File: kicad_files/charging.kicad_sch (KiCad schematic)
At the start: 2 parts, among them U2 BQ24650, U3 TL431DBZ

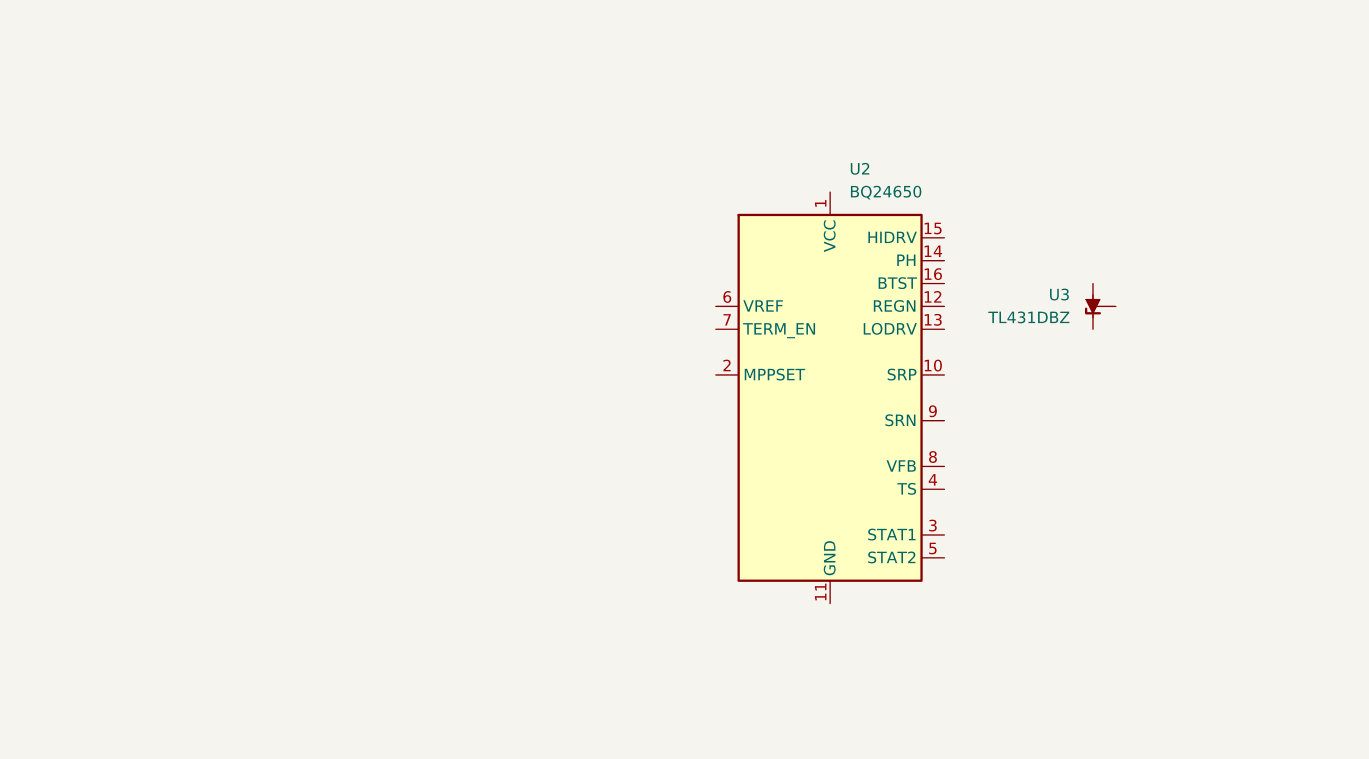
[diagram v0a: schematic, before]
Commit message: Some progress on charging schematic
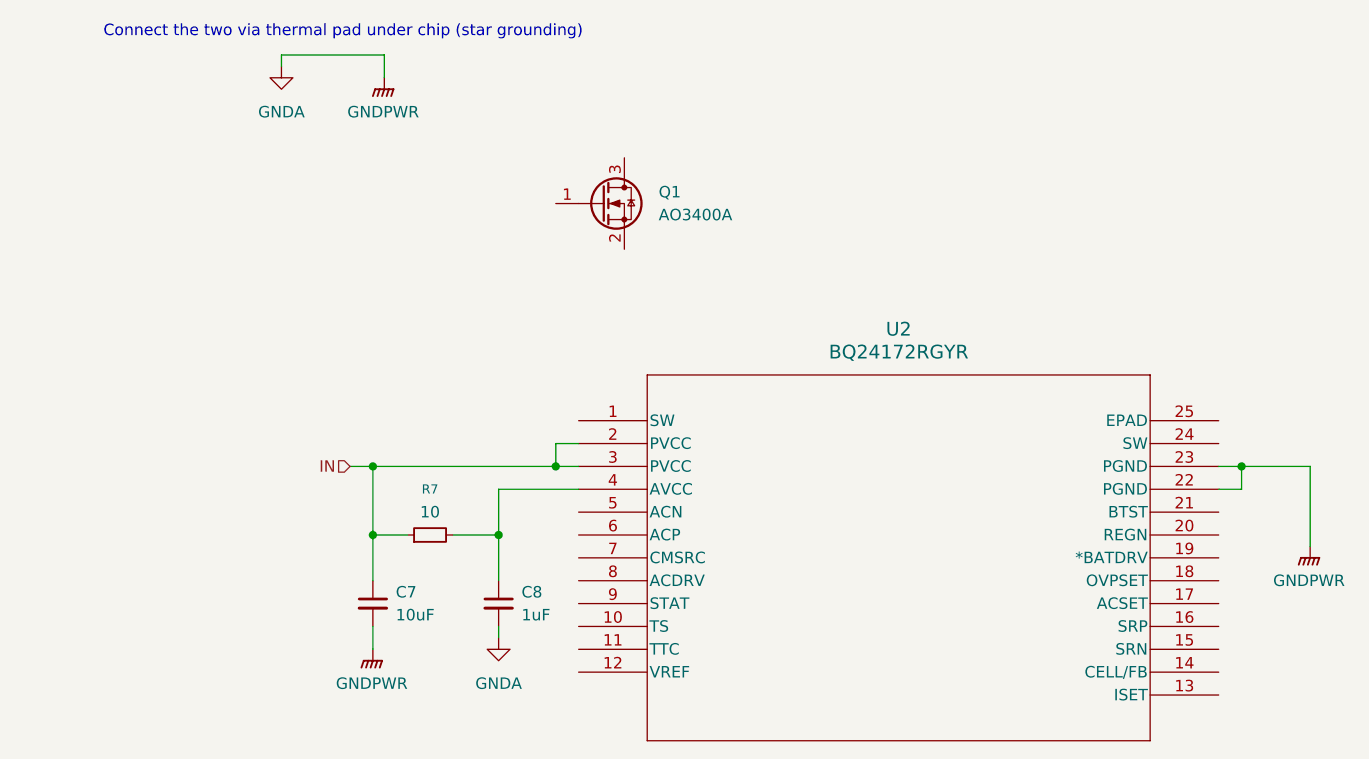
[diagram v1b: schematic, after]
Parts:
- removed U2: BQ24650, Package_DFN_QFN:Texas_RVA_VQFN-16-1EP_3.5x3.5mm_P0.5mm_EP2.14x2.14mm_ThermalVias, symbol Battery_Management:BQ24650
- removed U3: TL431DBZ, Package_TO_SOT_SMD:SOT-23, symbol Reference_Voltage:TL431DBZ
- added C7: 10uF, symbol Device:C_Small
- added C8: 1uF, symbol Device:C_Small
- added Q1: AO3400A, Package_TO_SOT_SMD:SOT-23, symbol Transistor_FET:AO3400A
- added R7: 10, symbol Device:R_Small
- added U2: BQ24172RGYR, RGY24_2P05X3P1, symbol !symbols:BQ24172RGYR
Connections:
- new net: C8.1, R7.2, U2.4 (AVCC)
- new net GNDA: C7.2, C8.2, U2.22 (PGND), U2.23 (PGND)
- new net IN: C7.1, R7.1, U2.2 (PVCC), U2.3 (PVCC)
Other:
- note added: "Connect the two via thermal pad under chip (star grounding)"

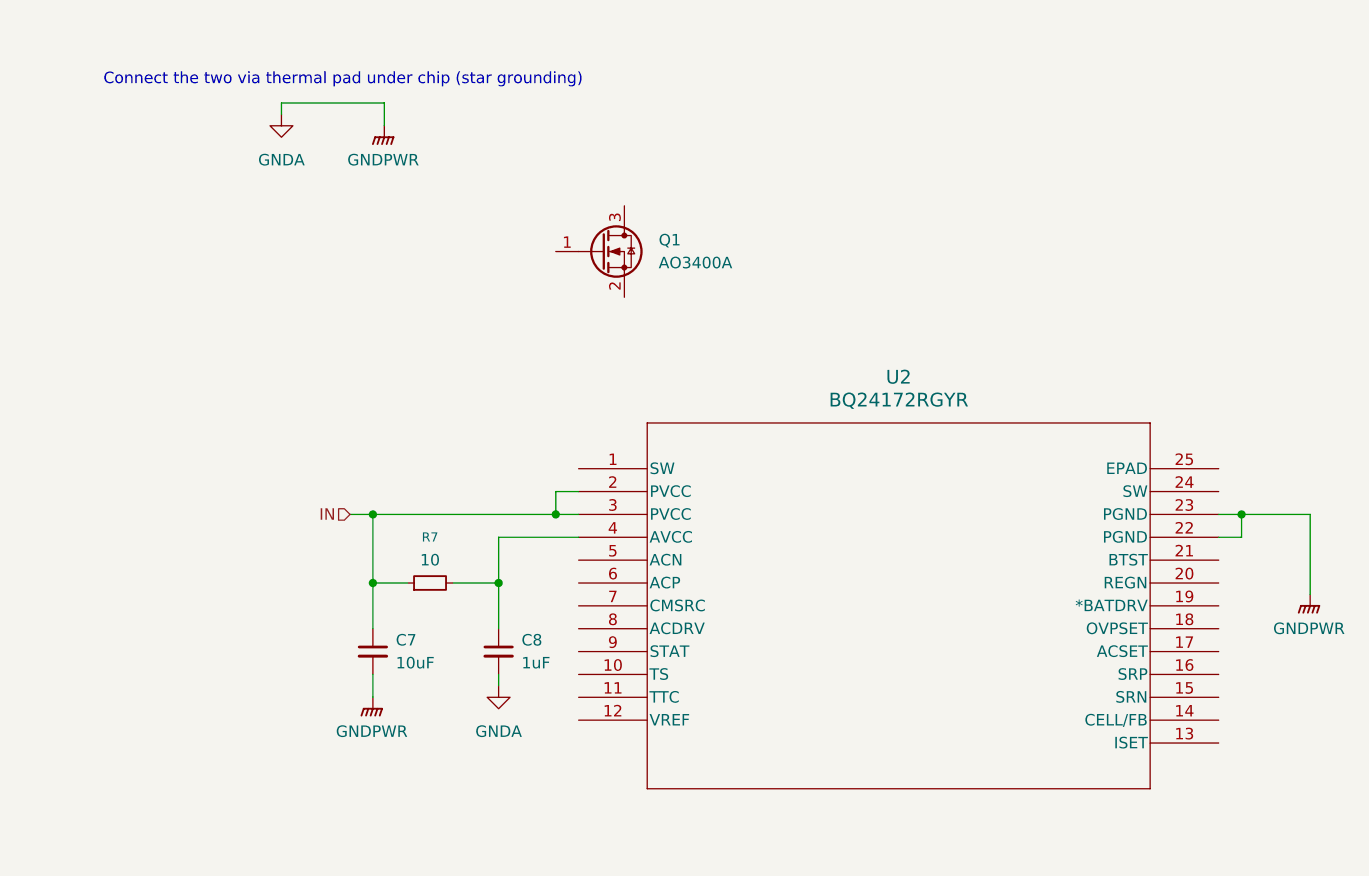
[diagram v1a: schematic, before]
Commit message: More progress on charging schematic
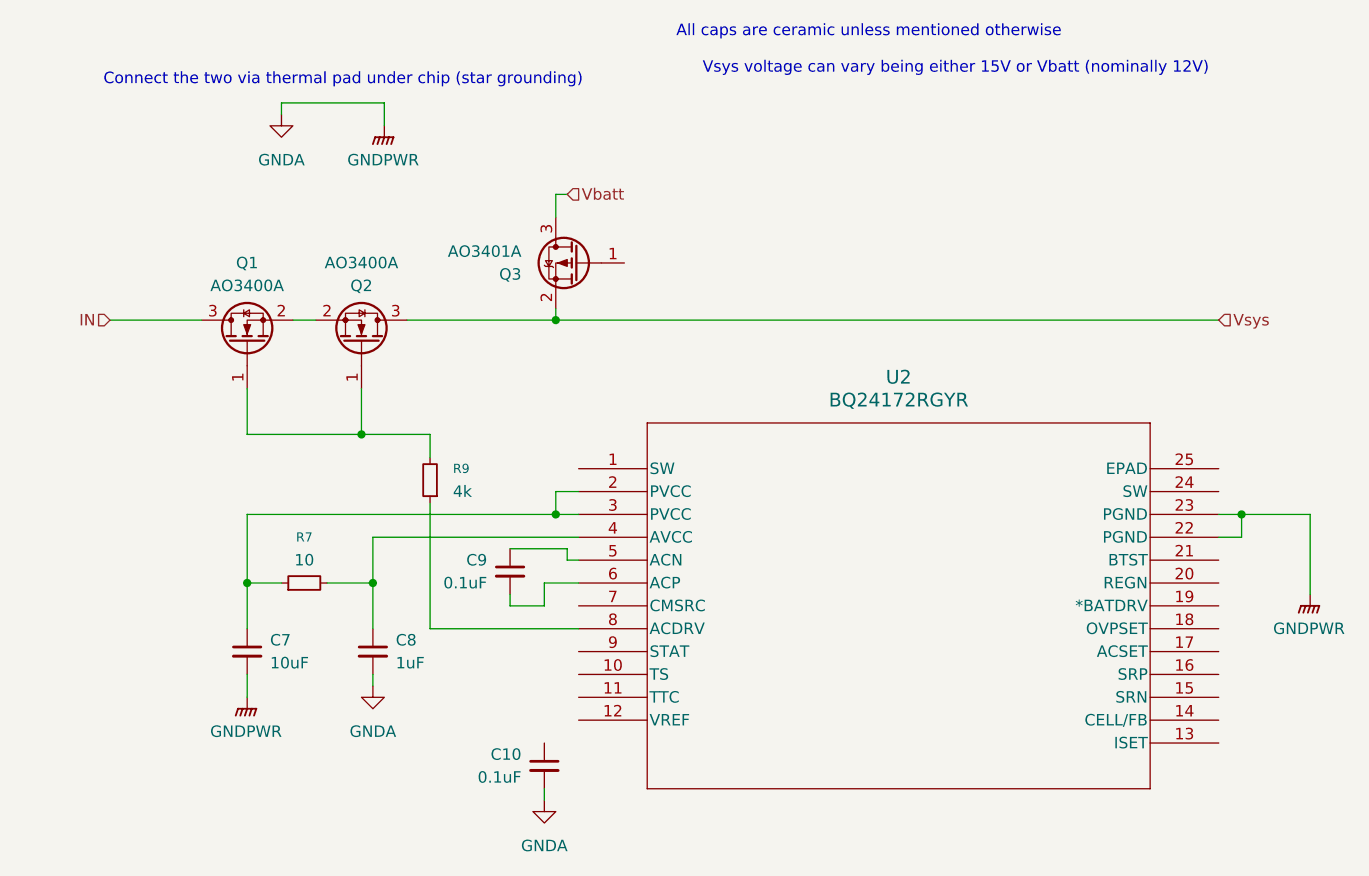
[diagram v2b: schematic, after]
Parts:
- added C10, C9: 0.1uF, symbol Device:C_Small
- added Q2: AO3400A, Package_TO_SOT_SMD:SOT-23, symbol Transistor_FET:AO3400A
- added Q3: AO3401A, Package_TO_SOT_SMD:SOT-23, symbol Transistor_FET:AO3401A
- added R9: 4k, symbol Device:R_Small
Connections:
- net GNDA: now also C10.2
- net IN: now also Q1.3 (D); no longer C7.1, R7.1, U2.2 (PVCC), U2.3 (PVCC)
- net at Q1.1 (G): now also Q2.1 (G), R9.2
- net at Q1.2 (S): now also Q2.2 (S)
- net at U2.5 (ACN): now also C9.1
- net at U2.6 (ACP): now also C9.2
- net at U2.8 (ACDRV): now also R9.1
- new net: C7.1, R7.1, U2.2 (PVCC), U2.3 (PVCC)
- new net Vbatt: Q3.3 (D)
- new net Vsys: Q2.3 (D), Q3.2 (S)
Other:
- note added: "All caps are ceramic unless mentioned otherwise"
- note added: "Vsys voltage can vary being either 15V or Vbatt (nominally 12V)"
- moved on the sheet: C7, C8, Q1, R7

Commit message: added cypd to one sheet
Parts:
- added U3: CYPD3177-24LQ, Package_DFN_QFN:QFN-24-1EP_4x4mm_P0.5mm_EP2.75x2.75mm, symbol CYPD3177-24LQ:CYPD3177-24LQ
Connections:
- new net: U3.19 (GND), U3.22 (GND), U3.25 (GND)
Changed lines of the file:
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@@
 	(version 20260306)
 	(generator "eeschema")
-	(generator_version "10.0")
+	(generator_version "10.99")
 	(paper "A4")
 	(text "Connect the two via thermal pad under chip (star grounding)"
@@
 					(unit 1)
 				)
+			)
+		)
+	)
+	(symbol
+		(lib_id "CYPD3177-24LQ:CYPD3177-24LQ")
+		(at 105.41 147.32 0)
+		(unit 1)
+		(body_style 1)
+		(exclude_from_sim no)
+		(in_bom yes)
+		(on_board yes)
+		(in_pos_files yes)
+		(dnp no)
+		(fields_autoplaced yes)
+		(property "Reference" "U3"
+			(at 107.5533 170.18 0)
+			(show_name no)
+			(do_not_autoplace no)
+			(effects
+				(font
+					(size 1.27 1.27)
+				)
+				(justify left)
+			)
+		)
+		(property "Value" "CYPD3177-24LQ"
+			(at 107.5533 172.72 0)
+			(show_name no)
+			(do_not_autoplace no)
+			(effects
+				(font
+					(size 1.27 1.27)
+				)
+				(justify left)
+			)
+		)
+		(property "Footprint" "Package_DFN_QFN:QFN-24-1EP_4x4mm_P0.5mm_EP2.75x2.75mm"
+			(at 105.41 147.32 0)
+			(hide yes)
+			(show_name no)
+			(do_not_autoplace no)
+			(effects
+				(font
+					(size 1.27 1.27)
+				)
+			)
+		)
+		(property "Datasheet" "https://www.infineon.com/dgdl/Infineon-EZ-PD_BCR_Datasheet_USB_Type-C_Port_Controller_for_Power_Sinks-DataSheet-v03_00-EN.pdf?fileId=8ac78c8c7d0d8da4017d0ee7ce9d70ad"
+			(at 105.41 147.32 0)
+			(hide yes)
+			(show_name no)
+			(do_not_autoplace no)
+			(effects
+				(font
+					(size 1.27 1.27)
+				)
+			)
+		)
+		(property "Description" "Stand-alone USB PD controller (with sink Auto-run mode), QFN-24"
+			(at 105.41 147.32 0)
+			(hide yes)
+			(show_name no)
+			(do_not_autoplace no)
+			(effects
+				(font
+					(size 1.27 1.27)
+				)
+			)
+		)
+		(pin "17"
+		)
+		(pin "18"
+		)
+		(pin "16"
+		)
+		(pin "12"
+		)
+		(pin "22"
+		)
+		(pin "4"
+		)
+		(pin "3"
+		)
+		(pin "2"
+		)
+		(pin "14"
+		)
+		(pin "7"
+		)
+		(pin "6"
+		)
+		(pin "5"
+		)
+		(pin "8"
+		)
+		(pin "25"
+		)
+		(pin "10"
+		)
+		(pin "20"
+		)
+		(pin "19"
+		)
+		(pin "21"
+		)
+		(pin "15"
+		)
+		(pin "9"
+		)
+		(pin "1"
+		)
+		(pin "11"
+		)
+		(pin "13"
+		)
+		(pin "23"
+		)
+		(pin "24"
+		)
+		(instances
+			(project "sodiumBMS"
+				(path "/fcdd2084-f4ec-4b1b-b9ac-497c327c0303/1b7ae7cb-6ce5-4b44-9aa9-df27edf3853f"
+					(reference "U3")
+					(unit 1)
+				)

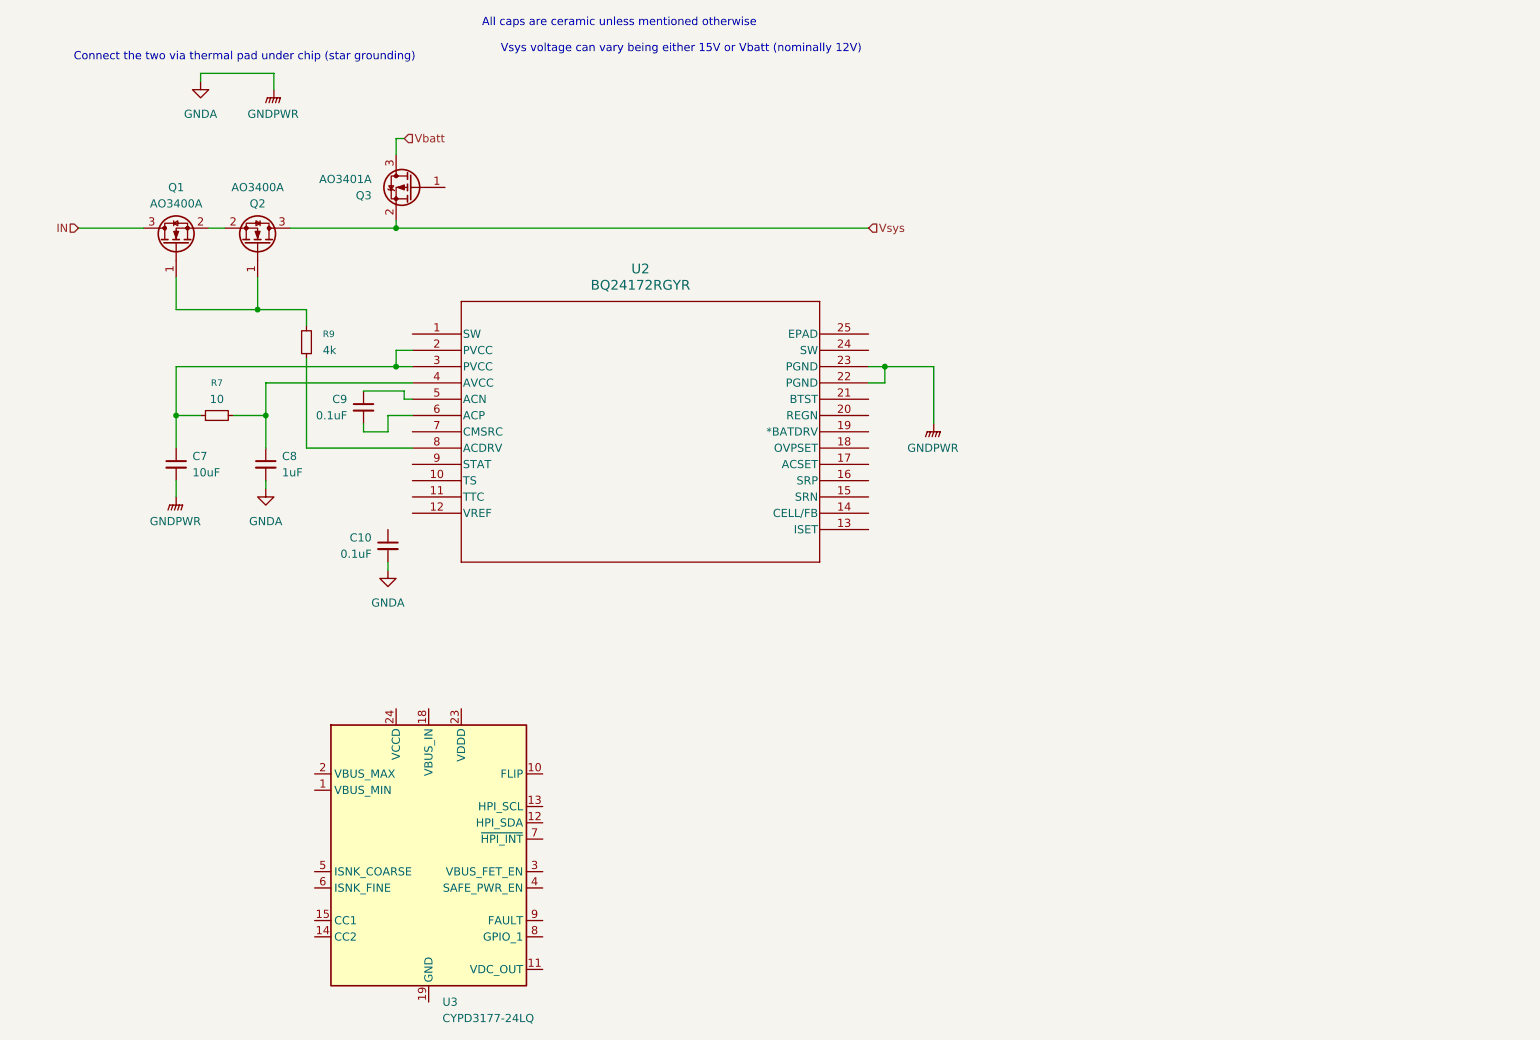
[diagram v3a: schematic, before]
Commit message: just copying the reference schematic from cypd3177 datasheet
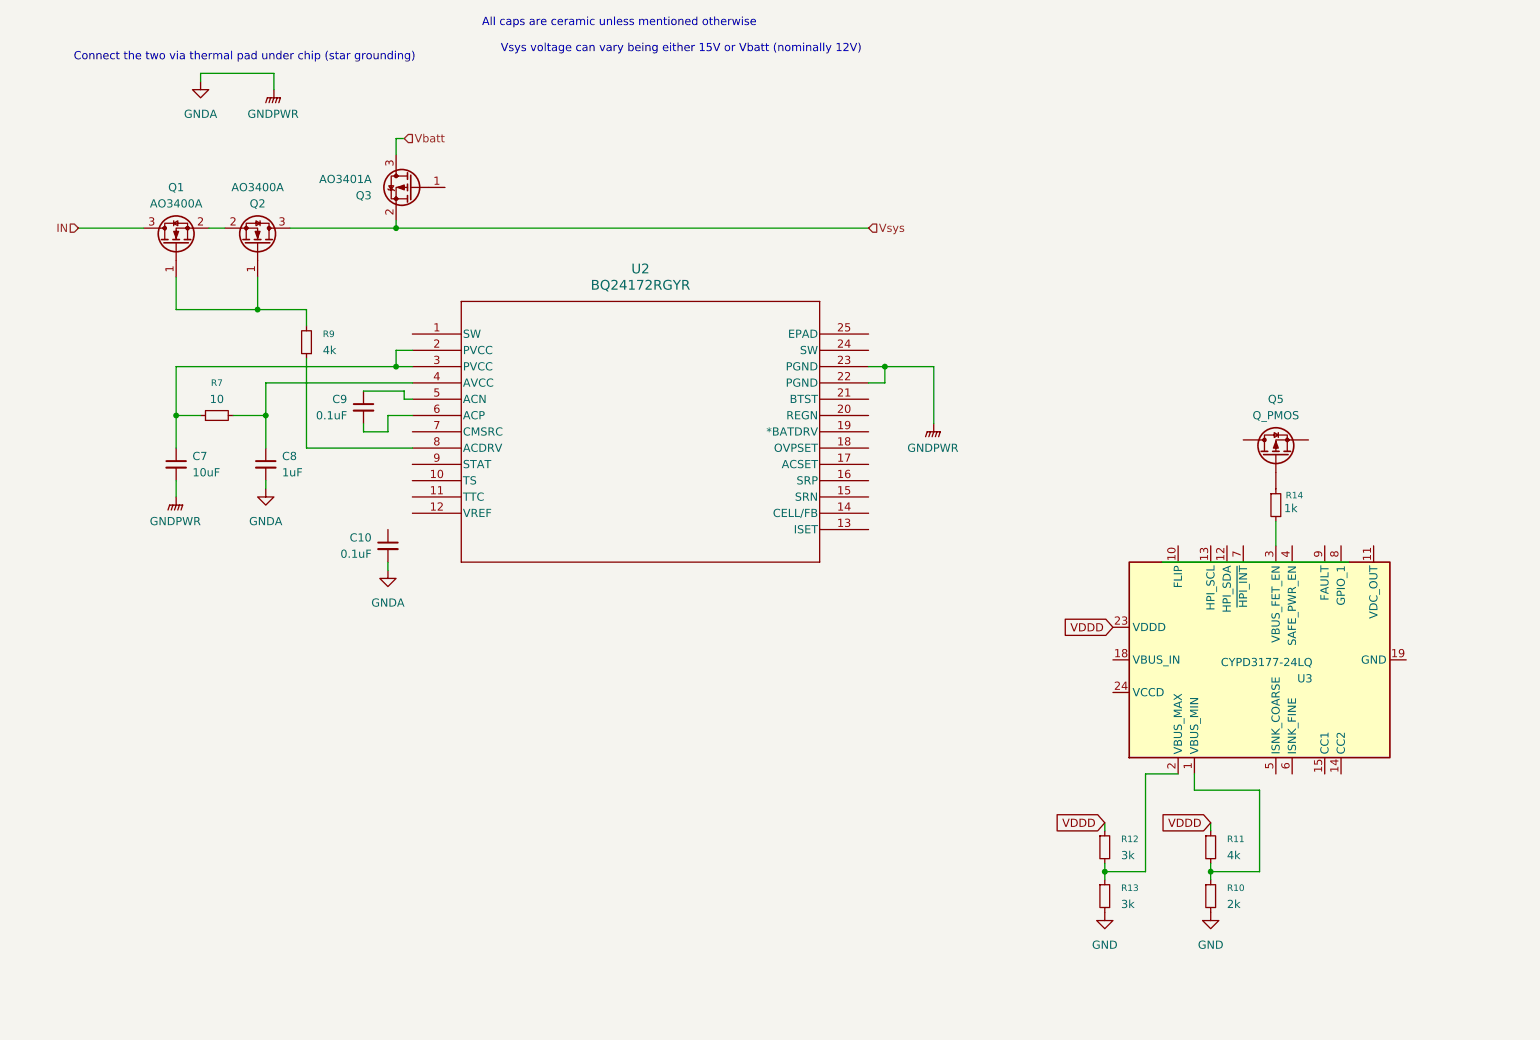
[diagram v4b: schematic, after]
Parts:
- added Q5: Q_PMOS, symbol Q_PMOS:Q_PMOS
- added R10: 2k, symbol R_Small:R_Small
- added R11: 4k, symbol R_Small:R_Small
- added R12, R13: 3k, symbol R_Small:R_Small
- added R14: 1k, symbol R_Small:R_Small
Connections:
- net at U3.1 (VBUS_MIN): now also R10.1, R11.2
- net at U3.2 (VBUS_MAX): now also R12.2, R13.1
- net VDDD: now reaches U3.23 (VDDD)
- net VDDD: now also R11.1, R12.1
- net at U3.3 (VBUS_FET_EN): now also R14.2
- new net: Q5.G, R14.1
- new net GND: R10.2, R13.2
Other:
- moved on the sheet: U3

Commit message: not much
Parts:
- added R15, R26: 3k, symbol R_Small:R_Small
- added R27: 4k, symbol R_Small:R_Small
- added R28: 2k, symbol R_Small:R_Small
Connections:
- net GND: now also U3.19 (GND), U3.22 (GND), U3.25 (GND), R26.2, R28.2
- net VDDD: now also R15.1, R27.1
- net at U3.5 (ISNK_COARSE): now also R15.2, R26.1
- net at U3.6 (ISNK_FINE): now also R27.2, R28.1

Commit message: added some connections for the PD controller
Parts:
- added C11: 3uF, symbol C_Small:C_Small
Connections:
- net GND: now also C11.2
- net SDA: now reaches U3.12 (HPI_SDA)
- net SCL: now reaches U3.13 (HPI_SCL)
- net CC2: now reaches U3.14 (CC2)
- net CC1: now reaches U3.15 (CC1)
- net VBUS_IN: now reaches U3.18 (VBUS_IN)
- net VBUS_IN: now also C11.1
